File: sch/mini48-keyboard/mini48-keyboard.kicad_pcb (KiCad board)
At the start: 2 copper layers, 233 x 81 mm, 97 parts, among them SW1 SW_Push, SW10 SW_Push, SW11 SW_Push, SW12 SW_Push, SW13 SW_Push, SW14 SW_Push, SW15 SW_Push, SW16 SW_Push, SW17 SW_Push, SW18 SW_Push, SW19 SW_Push, SW2 SW_Push, SW20 SW_Push, SW21 SW_Push, SW22 SW_Push, SW23 SW_Push, SW24 SW_Push, SW25 SW_Push, SW26 SW_Push, SW27 SW_Push, SW28 SW_Push, SW29 SW_Push, SW3 SW_Push, SW30 SW_Push, SW31 SW_Push, SW32 SW_Push, SW33 SW_Push, SW34 SW_Push, SW35 SW_Push, SW36 SW_Push, SW37 SW_Push, SW38 SW_Push, SW39 SW_Push, SW4 SW_Push, SW40 SW_Push, SW41 SW_Push, SW42 SW_Push, SW43 SW_Push, SW44 SW_Push, SW45 SW_Push, SW46 SW_Push, SW47 SW_Push, SW48 SW_Push, SW5 SW_Push, SW6 SW_Push, SW7 SW_Push, SW8 SW_Push, SW9 SW_Push

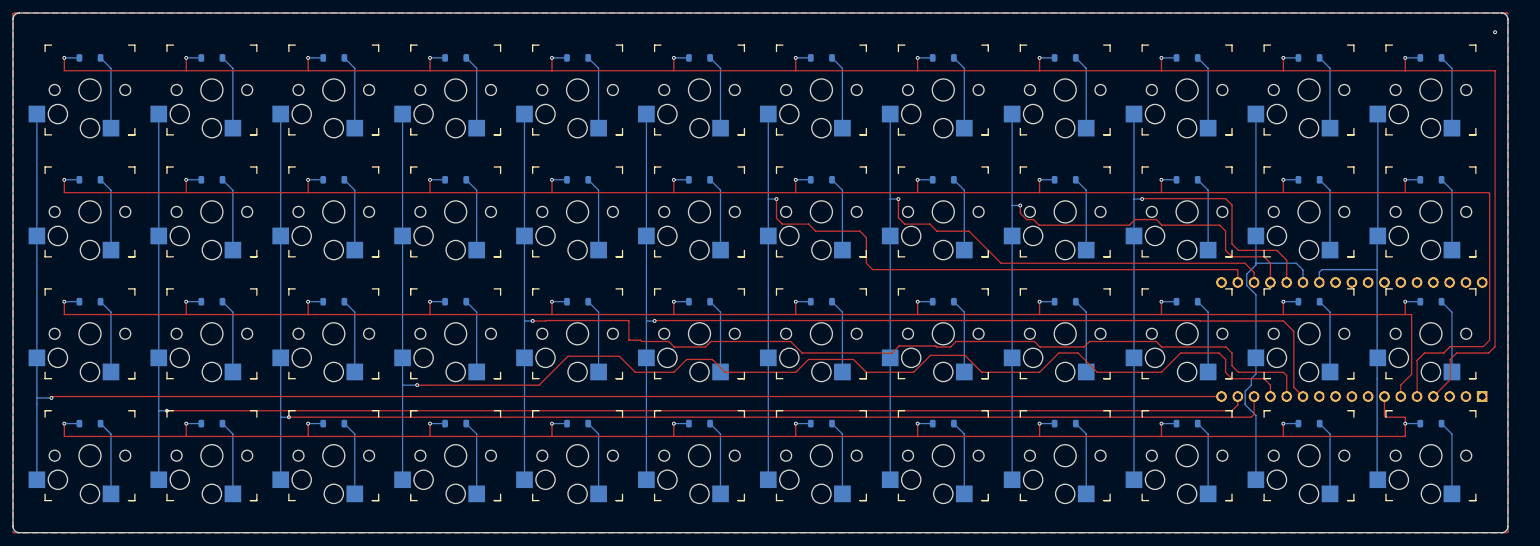
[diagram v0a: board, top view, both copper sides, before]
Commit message: 外形の微調整を行いました。 GNDベタにビアを打ちました。 余分なキーを切り離せるように、基板にスリットをいれました。
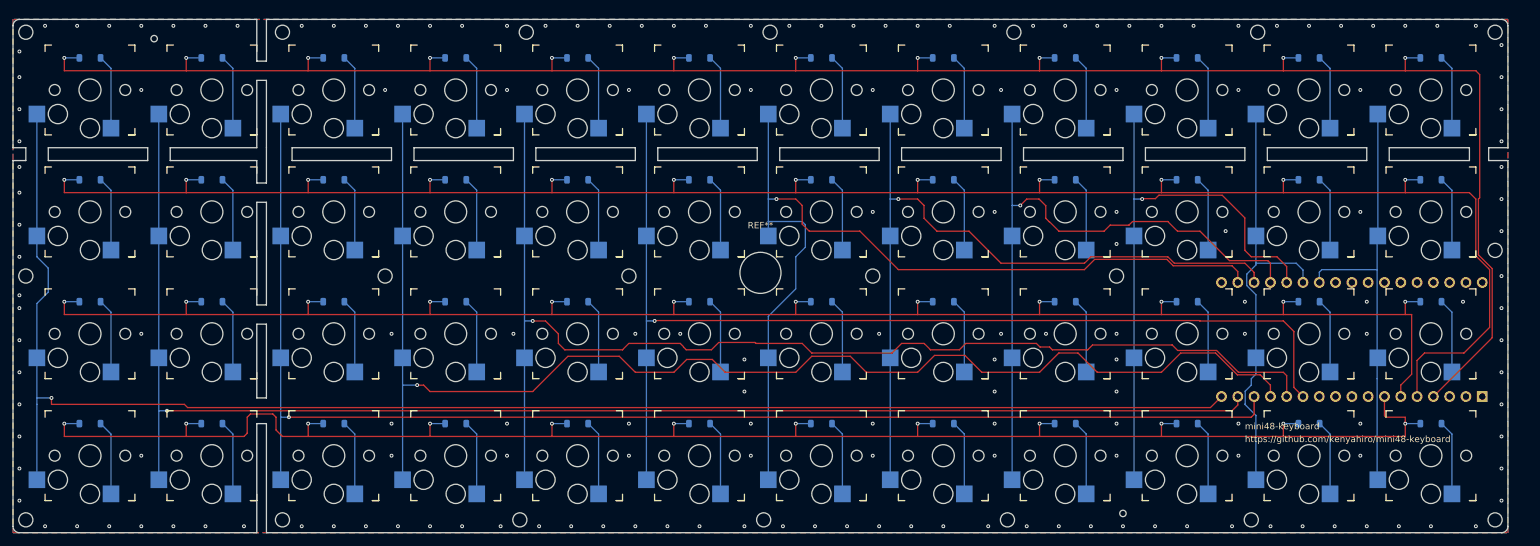
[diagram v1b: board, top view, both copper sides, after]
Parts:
- added REF**: MountingHole_2.2mm_M2, MountingHole:MountingHole_2.2mm_M2, F.Cu at (171.0, 93.0)
- added REF**: MountingHole_2.2mm_M2, MountingHole:MountingHole_2.2mm_M2, F.Cu at (230.0, 131.0)
- added REF**: MountingHole_2.2mm_M2, MountingHole:MountingHole_2.2mm_M2, F.Cu at (155.0, 55.0)
- added REF**: MountingHole_2.2mm_M2, MountingHole:MountingHole_2.2mm_M2, F.Cu at (268.0, 55.0)
- added REF**: MountingHole_2.2mm_M2, MountingHole:MountingHole_2.2mm_M2, F.Cu at (268.0, 89.0)
- added REF**: MountingHole_2.2mm_M2, MountingHole:MountingHole_2.2mm_M2, F.Cu at (231.0, 55.0)
- added REF**: MountingHole_2.2mm_M2, MountingHole:MountingHole_2.2mm_M2, F.Cu at (209.0, 93.0)
- added REF**: MountingHole_2.2mm_M2, MountingHole:MountingHole_2.2mm_M2, F.Cu at (39.0, 131.0)
- added REF**: MountingHole_2.2mm_M2, MountingHole:MountingHole_2.2mm_M2, F.Cu at (117.0, 55.0)
- added REF**: MountingHole_2.2mm_M2, MountingHole:MountingHole_2.2mm_M2, F.Cu at (133.0, 93.0)
- added REF**: MountingHole_6.4mm_M6, MountingHole:MountingHole_6.4mm_M6, F.Cu at (153.5, 92.5)
- added REF**: MountingHole_2.2mm_M2, MountingHole:MountingHole_2.2mm_M2, F.Cu at (79.0, 55.0)
- added REF**: MountingHole_2.2mm_M2, MountingHole:MountingHole_2.2mm_M2, F.Cu at (79.0, 131.0)
- added REF**: MountingHole_2.2mm_M2, MountingHole:MountingHole_2.2mm_M2, F.Cu at (116.0, 131.0)
- added REF**: hole1mm, my_keyswitch:hole1mm, B.Cu at (59.0, 56.0)
- added REF**: hole1mm, my_keyswitch:hole1mm, B.Cu at (210.0, 130.0)
- added REF**: MountingHole_2.2mm_M2, MountingHole:MountingHole_2.2mm_M2, F.Cu at (193.0, 55.0)
- added REF**: MountingHole_2.2mm_M2, MountingHole:MountingHole_2.2mm_M2, F.Cu at (39.0, 55.0)
- added REF**: MountingHole_2.2mm_M2, MountingHole:MountingHole_2.2mm_M2, F.Cu at (268.0, 131.0)
- added REF**: MountingHole_2.2mm_M2, MountingHole:MountingHole_2.2mm_M2, F.Cu at (39.0, 93.0)
- added REF**: MountingHole_2.2mm_M2, MountingHole:MountingHole_2.2mm_M2, F.Cu at (95.0, 93.0)
- added REF**: MountingHole_2.2mm_M2, MountingHole:MountingHole_2.2mm_M2, F.Cu at (154.0, 131.0)
- added REF**: MountingHole_2.2mm_M2, MountingHole:MountingHole_2.2mm_M2, F.Cu at (192.0, 131.0)
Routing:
- net /COL6: track 140.8 -> 149.7 mm
- net /ROW3: track 268.5 -> 274.1 mm
- net /ROW0: track 332.9 -> 328.0 mm
- net /COL0: track 241.7 -> 245.0 mm
- net /ROW1: track 315.5 -> 312.6 mm
- net /COL9: track 91.8 -> 91.1 mm
- net /COL4: track 188.6 -> 188.0 mm
- net GND: vias 1 -> 170
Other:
- board size 233 x 81 mm -> 233 x 80 mm
- board text added: "https://github.com/kenyahiro/mini48-keyboard"
- board text added: "mini48-keyboard"

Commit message: 基板のスリットをやめました。 基板外形の微調整を行いました。ネジ穴の位置の微調整を行いました。
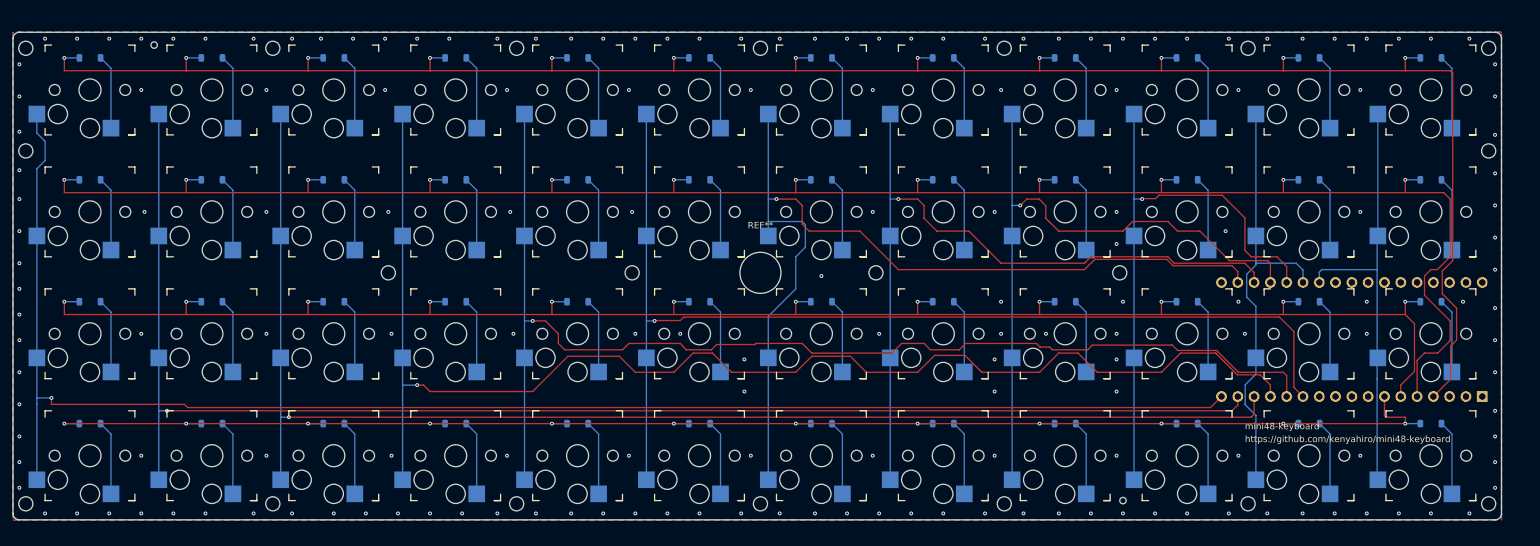
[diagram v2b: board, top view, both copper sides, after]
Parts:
- moved REF** 19.5 mm to (39.0, 73.5)
- moved REF** 15.5 mm to (267.0, 73.5)
- moved REF** 2.92 mm to (153.5, 57.5)
- moved REF** 2.92 mm to (229.5, 57.5)
- moved REF** 2.92 mm to (115.5, 57.5)
- moved REF** 2.92 mm to (77.5, 57.5)
- moved REF** 2.92 mm to (77.5, 128.5)
- moved REF** 2.92 mm to (191.5, 57.5)
- moved REF** 2.69 mm to (267.0, 57.5)
- moved REF** 2.69 mm to (267.0, 128.5)
- moved REF** 2.55 mm to (229.5, 128.5)
- moved REF** 2.55 mm to (115.5, 128.5)
- moved REF** 2.55 mm to (153.5, 128.5)
- moved REF** 2.55 mm to (191.5, 128.5)
- moved REF** 2.50 mm to (39.0, 128.5)
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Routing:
- net /ROW3: track 274.1 -> 244.5 mm
- net /ROW1: track 312.6 -> 306.6 mm
- net /ROW0: track 328.0 -> 322.2 mm
- net /COL3: track 209.5 -> 210.3 mm
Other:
- board size 233 x 80 mm -> 232 x 76 mm
